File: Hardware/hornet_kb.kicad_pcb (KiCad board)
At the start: 2 copper layers, 135 parts, among them J1 Conn_ST_STDC14, J10 USB_C_Receptacle_USB2.0, SW1 F7, SW10 8, SW11 9, SW12 0, SW13 -/_, SW14 +/=, SW15 BS, SW16 PAGE_DOWN, SW17 Y, SW18 U, SW19 I, SW2 F8, SW20 O, SW21 P, SW22 [, SW23 ], SW24 \, SW25 H, SW26 B, SW27 Space, SW28 J, SW29 N, SW3 F9, SW4 F10, SW5 F11, SW6 F12, SW7 DEL, SW8 PAGE_UP, SW9 7, U1 nRF52840

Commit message: added zander layout
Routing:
- net unconnected-(U1-NFC1/P0.09-PadL24): track 1.74 -> 0.00 mm
- net Net-(U1-XC1): track 0.99 -> 0.00 mm
- net unconnected-(U1-P1.07-PadP23): track 0.85 -> 0.00 mm
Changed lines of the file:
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@@
 		)
-	)
-	(segment
-		(start 153.4 115.9)
-		(end 154.1 115.2)
-		(width 0.2)
-		(layer "F.Cu")
-		(net 4)
-	)
-	(segment
-		(start 152.9 119.15)
-		(end 152.9 118.3)
-		(width 0.2)
-		(layer "F.Cu")
-		(net 153)
-	)
-	(segment
-		(start 155 118.4)
-		(end 155.1 118.3)
-		(width 0.2)
-		(layer "F.Cu")
-		(net 166)
-	)
-	(segment
-		(start 153.4 118.4)
-		(end 155 118.4)
-		(width 0.2)
-		(layer "F.Cu")
-		(net 166)
 	)
 	(embedded_fonts no)

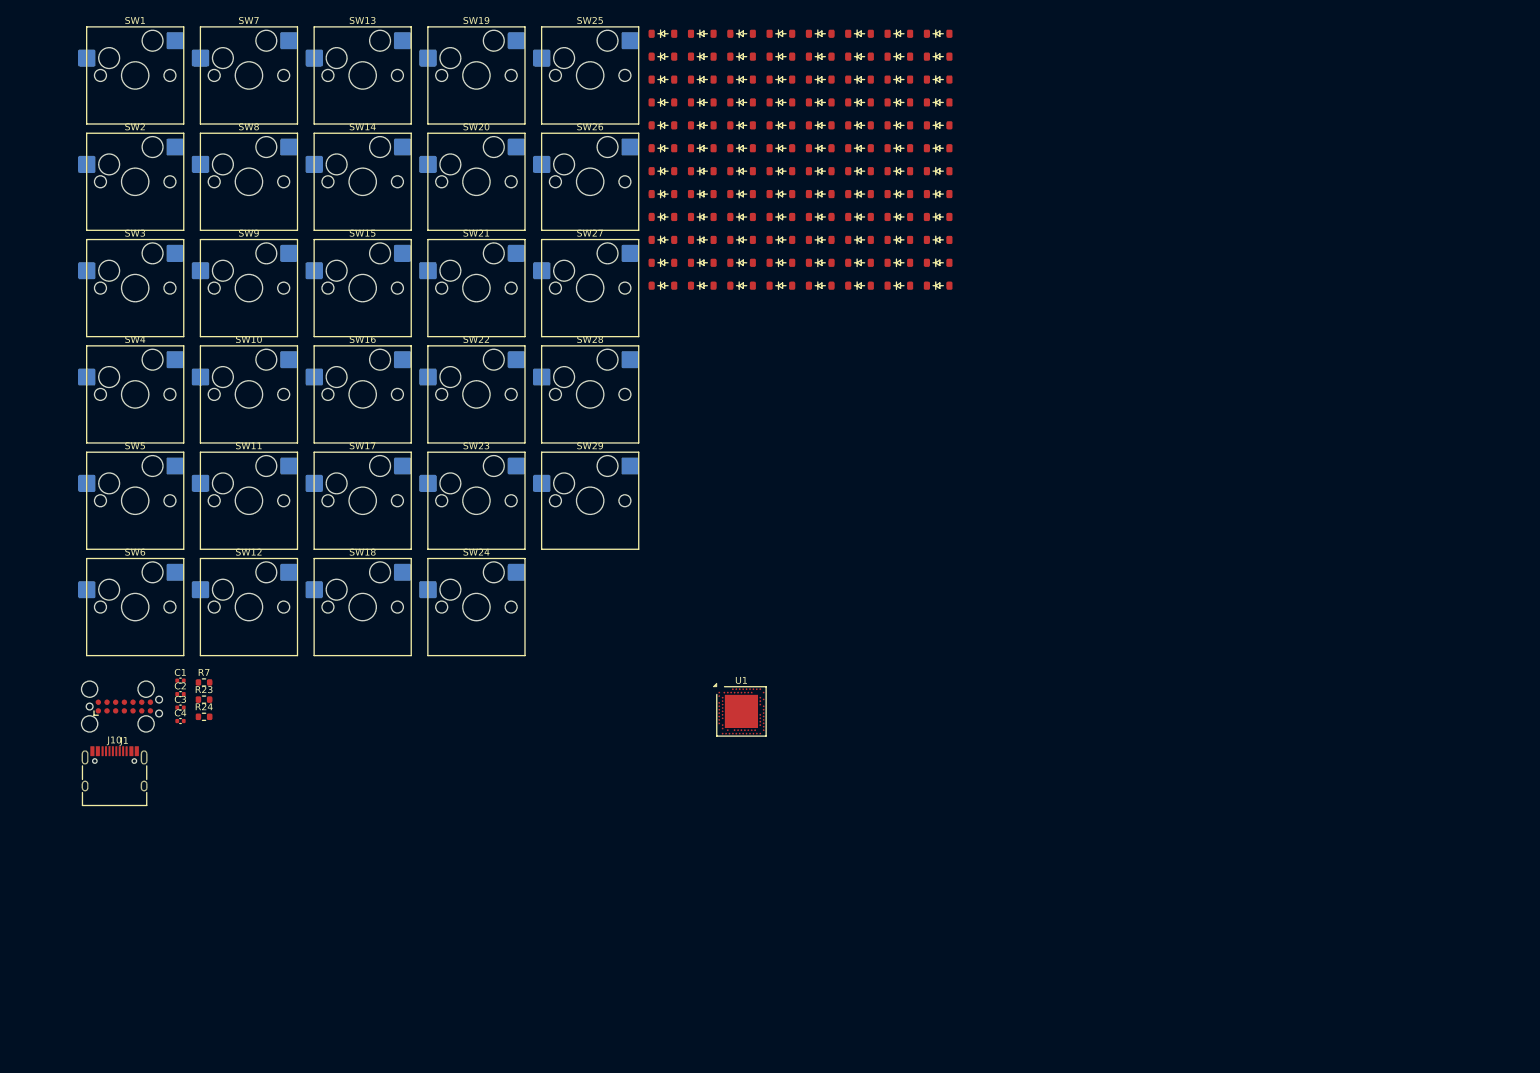
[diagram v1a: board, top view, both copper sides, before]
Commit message: Completed Final GUI Key Layout and PCB key layout draft
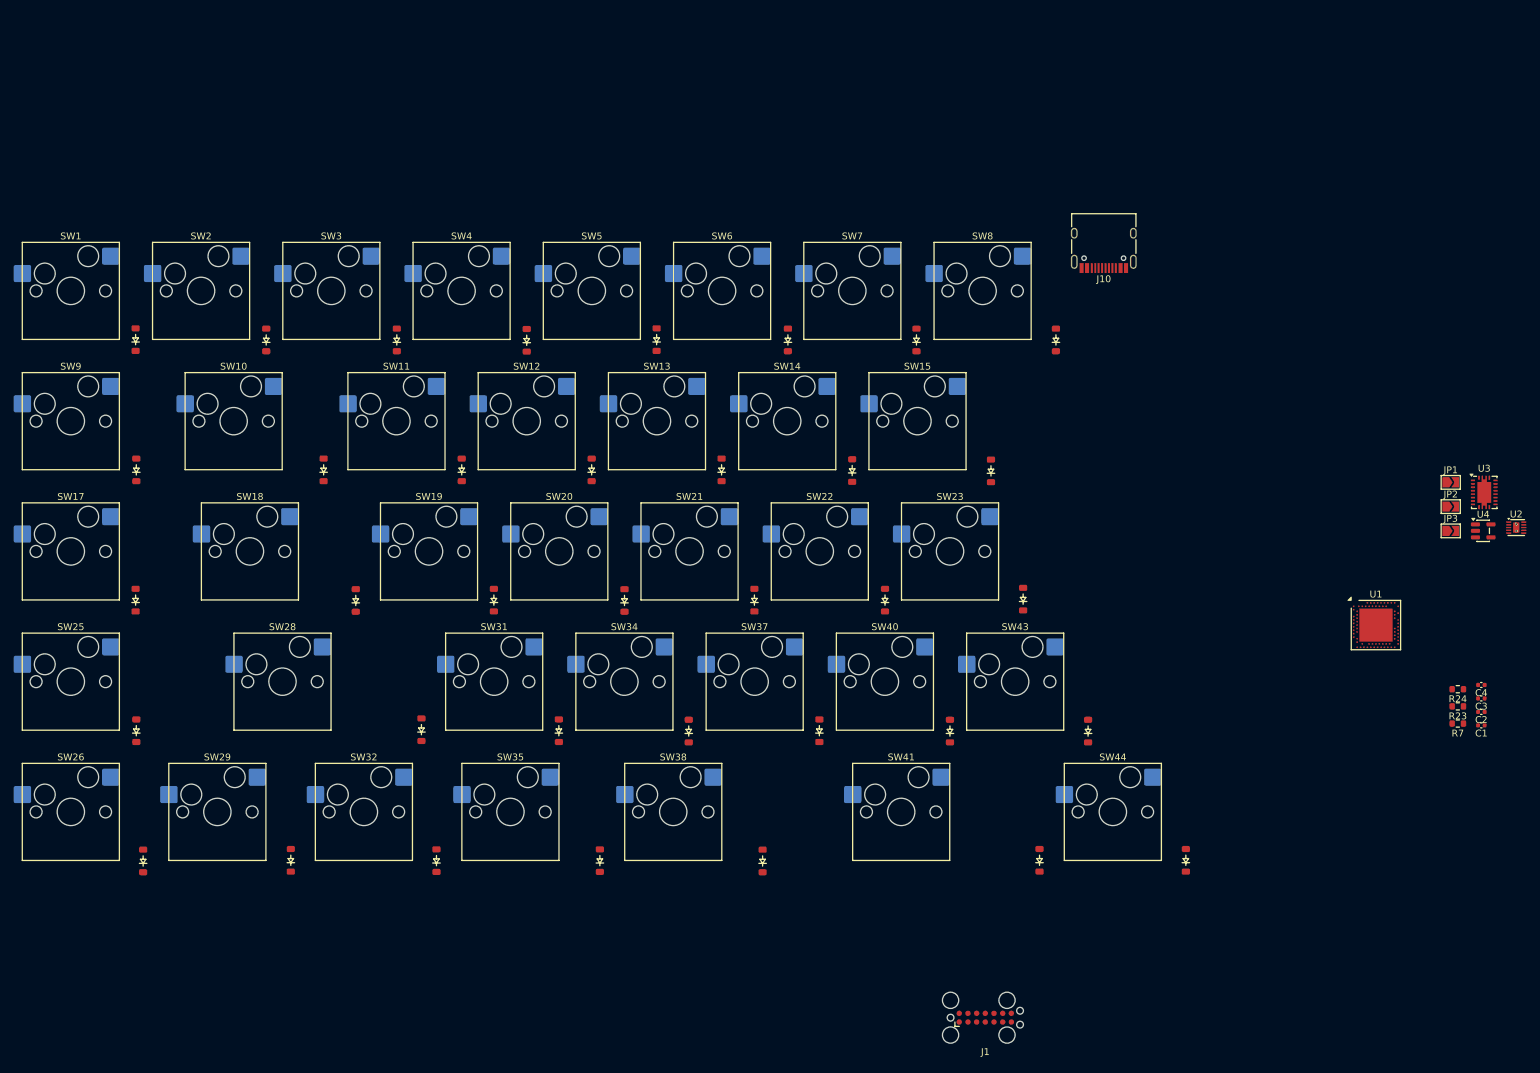
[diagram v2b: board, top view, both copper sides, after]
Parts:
- removed D16, D24, D27, D30, D33, D36, D39, D42, D45, D46, D47, D48, D49, D50, D51, D52, D53, D54, D55, D56, D57, D58, D59, D60, D61, D62, D63, D64, D65, D66, D67, D68, D69, D70, D71, D72, D73, D74, D75, D76, D77, D78, D79, D80, D81, D82, D83, D84, D85, D86, D87, D88, D89, D90, D91, D92, D93, D94, D95, D96: D, ScottoKeebs_Components:Diode_SOD-123
- removed SW16: PAGE_DOWN, ScottoKeebs_Hotswap:Hotswap_MX_1.00u
- removed SW24: \, ScottoKeebs_Hotswap:Hotswap_MX_1.50u
- removed SW27: Space, ScottoKeebs_Hotswap:Hotswap_MX_2.75u
- added JP1: USB_CHG_ENA1, Jumper:SolderJumper-2_P1.3mm_Open_TrianglePad1.0x1.5mm, F.Cu at (253.9, 85.2)
- added JP2: USB_CHG_ENA2, Jumper:SolderJumper-2_P1.3mm_Open_TrianglePad1.0x1.5mm, F.Cu at (253.9, 88.7)
- added JP3: Qi_CHG_ENA, Jumper:SolderJumper-2_P1.3mm_Open_TrianglePad1.0x1.5mm, F.Cu at (253.9, 92.2)
- added SW31: Z, ScottoKeebs_Hotswap:Hotswap_MX_1.00u, F.Cu at (114.0, 114.3)
- added SW32: WIN, ScottoKeebs_Hotswap:Hotswap_MX_1.00u, F.Cu at (94.9, 133.3)
- added SW34: X, ScottoKeebs_Hotswap:Hotswap_MX_1.00u, F.Cu at (133.0, 114.3)
- added SW35: FN, ScottoKeebs_Hotswap:Hotswap_MX_1.25u, F.Cu at (116.4, 133.3)
- added SW37: C, ScottoKeebs_Hotswap:Hotswap_MX_1.00u, F.Cu at (152.1, 114.3)
- added SW38: ALT, ScottoKeebs_Hotswap:Hotswap_MX_1.25u, F.Cu at (140.2, 133.3)
- added SW40: V, ScottoKeebs_Hotswap:Hotswap_MX_1.00u, F.Cu at (171.1, 114.3)
- added SW41: SPACE, ScottoKeebs_Hotswap:Hotswap_MX_2.25u, F.Cu at (173.5, 133.3)
- added SW43: B, ScottoKeebs_Hotswap:Hotswap_MX_1.00u, F.Cu at (190.2, 114.3)
- added SW44: DEL, ScottoKeebs_Hotswap:Hotswap_MX_1.00u, F.Cu at (204.5, 133.3)
- added U2: BQ24040, Package_DFN_QFN:Texas_DLH0010A_WSON-10-1EP_2.2x2mm_P0.4mm_EP0.9x1.5mm_ThermalVias, F.Cu at (263.5, 91.8)
- added U3: BQ51050BRHL, Package_DFN_QFN:Texas_VQFN-RHL-20, F.Cu at (258.8, 86.6)
- added U4: AP22814BW5, Package_TO_SOT_SMD:SOT-23-5, F.Cu at (258.6, 92.2)
- D1: value D -> ESC
- D2: value D -> ~/`
- D3: value D -> 1
- D4: value D -> 2
- D5: value D -> 3
- D6: value D -> 4
- D7: value D -> 5
- D8: value D -> 6
- SW1: value F7 -> ESC
- SW10: value 8 -> TAB; footprint ScottoKeebs_Hotswap:Hotswap_MX_1.00u -> ScottoKeebs_Hotswap:Hotswap_MX_1.50u
- SW11: value 9 -> Q
- SW12: value 0 -> W
- SW13: value -/_ -> E
- SW14: value +/= -> R
- SW15: value BS -> T; footprint ScottoKeebs_Hotswap:Hotswap_MX_2.00u -> ScottoKeebs_Hotswap:Hotswap_MX_1.00u
- SW17: value Y -> M1
- SW18: value U -> CAPS; footprint ScottoKeebs_Hotswap:Hotswap_MX_1.00u -> ScottoKeebs_Hotswap:Hotswap_MX_1.75u
- SW19: value I -> A
- SW2: value F8 -> `
- SW20: value O -> S
- SW21: value P -> D
- SW22: value [ -> F
- SW23: value ] -> G
- SW25: value H -> M2
- SW26: value B -> M3
- SW28: value J -> SHIFT; footprint ScottoKeebs_Hotswap:Hotswap_MX_1.00u -> ScottoKeebs_Hotswap:Hotswap_MX_2.25u
- SW29: value N -> CTRL; footprint ScottoKeebs_Hotswap:Hotswap_MX_1.00u -> ScottoKeebs_Hotswap:Hotswap_MX_1.25u
- SW3: value F9 -> 1
- SW4: value F10 -> 2
- SW5: value F11 -> 3
- SW6: value F12 -> 4
- SW7: value DEL -> 5
- SW8: value PAGE_UP -> 6
- SW9: value 7 -> M0
- moved C1 190.4 mm to (258.4, 120.7), turned to 180 degrees
- moved C4 190.3 mm to (258.4, 114.8), turned to 180 degrees
- moved C2 190.3 mm to (258.4, 118.7), turned to 180 degrees
- moved C3 190.3 mm to (258.4, 116.8), turned to 180 degrees
- moved R7 183.5 mm to (254.9, 120.4), turned to 180 degrees
- moved R24 183.4 mm to (254.9, 115.4), turned to 180 degrees
- moved R23 183.4 mm to (254.9, 117.9), turned to 180 degrees
- moved J10 164.7 mm to (203.1, 49.8), turned to 180 degrees
- moved D26 146.6 mm to (62.6, 140.5), turned to 90 degrees
- moved D25 135.0 mm to (61.6, 121.5), turned to 90 degrees
- moved J1 133.9 mm to (185.8, 163.4)
- moved D29 126.1 mm to (84.2, 140.4), turned to 90 degrees
- moved SW26 119.4 mm to (52.1, 133.3)
- moved D38 117.7 mm to (153.2, 140.5), turned to 90 degrees
- moved SW25 116.7 mm to (52.1, 114.3)
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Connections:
- J1 pad 3: unconnected-(J1-VCC-Pad3) -> VDD1
- J10 pad A4: +5V -> VBUS
- J10 pad A9: +5V -> VBUS
- J10 pad B4: +5V -> VBUS
- J10 pad B9: +5V -> VBUS
- R7 pad 1: +3.3V -> VDD1
- U1 pad A14: unconnected-(U1-P1.15-PadA14) -> /COMPRT_TX
- U1 pad A22: Net-(U1-VDD-PadA22) -> VDD1
- U1 pad AB2: unconnected-(U1-DCCH-PadAB2) -> Net-(U1-DCCH)
- U1 pad AC17: unconnected-(U1-P0.21-PadAC17) -> R_COL_6
- U1 pad AC19: unconnected-(U1-P0.23-PadAC19) -> R_COL_4
- U1 pad AC21: unconnected-(U1-P0.25-PadAC21) -> R_COL_2
- U1 pad AC5: unconnected-(U1-DECUSB-PadAC5) -> Net-(U1-DECUSB)
- U1 pad AD14: Net-(U1-VDD-PadA22) -> VDD1
- U1 pad AD18: unconnected-(U1-P0.22-PadAD18) -> R_COL_5
- U1 pad AD2: unconnected-(U1-VBUS-PadAD2) -> VBUS
- U1 pad AD20: unconnected-(U1-P0.24-PadAD20) -> R_COL_3
- U1 pad AD23: Net-(U1-VDD-PadA22) -> VDD1
- U1 pad B1: Net-(U1-VDD-PadA22) -> VDD1
- U1 pad B15: unconnected-(U1-P1.14-PadB15) -> /COMPRT_RX
- U1 pad B3: unconnected-(U1-DCC-PadB3) -> Net-(U1-DCC)
- U1 pad B5: unconnected-(U1-DEC4-PadB5) -> Net-(U1-DEC4)
- U1 pad C1: unconnected-(U1-DEC1-PadC1) -> Net-(U1-DEC1)
- U1 pad D23: unconnected-(U1-DEC3-PadD23) -> Net-(U1-DEC3)
- U1 pad E24: unconnected-(U1-DEC6-PadE24) -> Net-(U1-DEC4)
- U1 pad F23: GND1 -> VSS_pa
- U1 pad G1: unconnected-(U1-P0.26-PadG1) -> R_COL_1
- U1 pad H2: unconnected-(U1-P0.27-PadH2) -> R_COL_0
- U1 pad H23: unconnected-(U1-ANT-PadH23) -> Net-(U1-ANT)
- U1 pad N24: unconnected-(U1-DEC5-PadN24) -> Net-(U1-DEC5)
- U1 pad R24: unconnected-(U1-P1.06-PadR24) -> R_ROW_5
- U1 pad T23: unconnected-(U1-P1.05-PadT23) -> R_ROW_4
- U1 pad U24: unconnected-(U1-P1.04-PadU24) -> R_ROW_3
- U1 pad V23: unconnected-(U1-P1.03-PadV23) -> R_ROW_2
- U1 pad W1: Net-(U1-VDD-PadA22) -> VDD1
- U1 pad W24: unconnected-(U1-P1.02-PadW24) -> R_ROW_1
- U1 pad Y2: unconnected-(U1-VDDH-PadY2) -> VDD1
- U1 pad Y23: unconnected-(U1-P1.01-PadY23) -> R_ROW_0
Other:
- board text added: "For the sake of price and challenge (mainly price...), This design will be a SINGLE sided assembly with all parts mounted on the REAR end of the board alongside the hotswap sockets"
- board text added: "Try and make this space as small as possible"

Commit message: added stabilizers to layout
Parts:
- added REF**: Stabilizer_MX_2.00u, ScottoKeebs_Stabilizer:Stabilizer_MX_2.00u, F.Cu at (83.0, 114.3)
- added REF**: Stabilizer_MX_2.00u, ScottoKeebs_Stabilizer:Stabilizer_MX_2.00u, F.Cu at (173.5, 133.3)
- moved J1 86.4 mm to (237.2, 94.0), turned to 90 degrees
- moved U1 24.2 mm to (220.3, 114.5)
